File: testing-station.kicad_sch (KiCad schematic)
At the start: 12 parts, among them J1 pyranometer, J2 anemometer, J3 AM2315C, J4 FPC connector, U1 TBA_1-0519

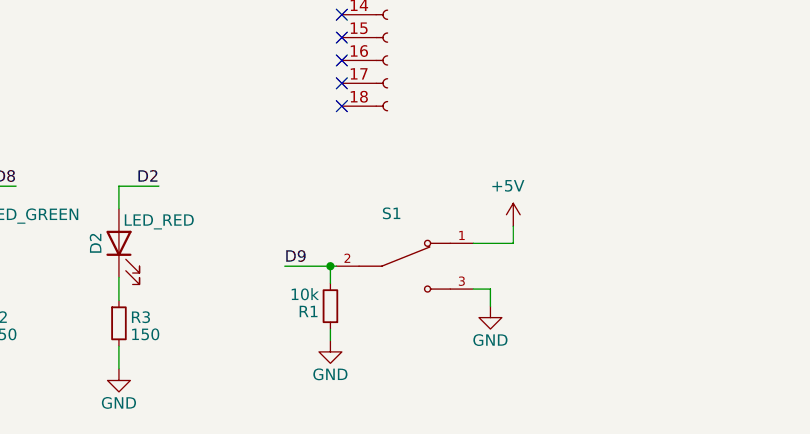
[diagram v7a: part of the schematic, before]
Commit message: added missing external files for PSU and switch + footprints update
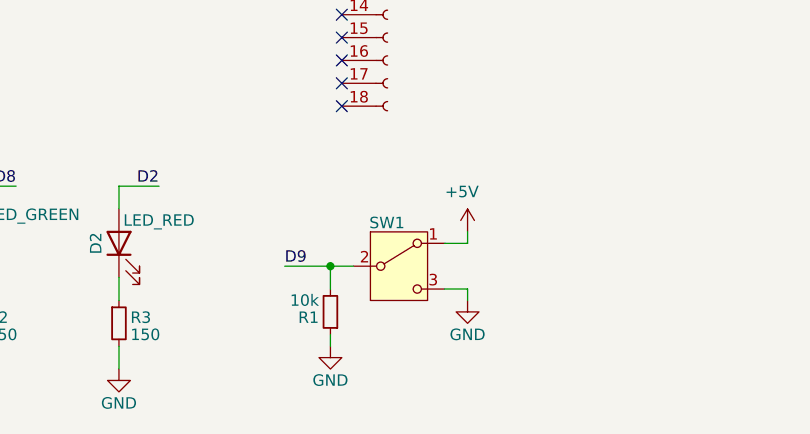
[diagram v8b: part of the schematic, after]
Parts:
- J1, J3: footprint custom_components:screw_terminal_4pin -> TerminalBlock:TerminalBlock_bornier-4_P5.08mm
- J2: footprint custom_components:screw_terminal_3pin -> TerminalBlock:TerminalBlock_bornier-3_P5.08mm
- SW1: renamed from S1; footprint 500SSP1S2M2QEA:SW_500SSP1S2M2QEA -> external_footprints:500SSP1S2M2QEA; symbol 500SSP1S2M2QEA:500SSP1S2M2QEA -> Switch:SW_SPDT
- U1: footprint TBA_1-0519:CONV_TBA_1-0519 -> external_footprints:TBA_1-0519
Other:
- moved on the sheet: R1, SW1
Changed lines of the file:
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@@
 	(wire
 		(pts
-			(xy 131.445 152.4) (xy 135.89 152.4)
-		)
-		(stroke
-			(width 0)
-			(type default)
-			(color 255 0 0 1)
-		)
-	)
-	(wire
-		(pts
 			(xy 110.49 109.22) (xy 116.84 109.22)
 		)
@@
 	(wire
 		(pts
-			(xy 115.57 154.94) (xy 116.205 154.94)
+			(xy 128.27 157.48) (xy 130.81 157.48)
 		)
 		(stroke
 			(width 0)
 			(type default)
-			(color 0 0 255 1)
+			(color 0 0 0 1)
 		)
 	)
@@
 	(wire
 		(pts
-			(xy 131.445 157.48) (xy 133.35 157.48)
-		)
-		(stroke
-			(width 0)
-			(type default)
-			(color 0 0 0 1)
-		)
-	)
-	(wire
-		(pts
 			(xy 110.49 50.8) (xy 116.84 50.8)
 		)
@@
 	(wire
 		(pts
+			(xy 115.57 154.94) (xy 115.57 157.48)
+		)
+		(stroke
+			(width 0)
+			(type default)
+			(color 0 0 255 1)
+		)
+	)
+	(wire
+		(pts
 			(xy 83.82 69.85) (xy 88.9 69.85)
 		)
@@
 	(wire
 		(pts
-			(xy 135.89 152.4) (xy 135.89 150.495)
+			(xy 130.81 152.4) (xy 130.81 151.13)
 		)
 		(stroke
@@
 	(wire
 		(pts
-			(xy 115.57 163.195) (xy 115.57 161.925)
+			(xy 115.57 163.83) (xy 115.57 162.56)
 		)
 		(stroke
@@
 	(wire
 		(pts
-			(xy 49.53 102.87) (xy 44.45 102.87)
+			(xy 115.57 154.94) (xy 118.11 154.94)
+		)
+		(stroke
+			(width 0)
+			(type default)
+			(color 0 0 255 1)
+		)
+	)
+	(wire
+		(pts
+			(xy 128.27 152.4) (xy 130.81 152.4)
 		)
 		(stroke
@@
 	(wire
 		(pts
-			(xy 114.3 93.98) (xy 116.84 93.98)
+			(xy 49.53 102.87) (xy 44.45 102.87)
 		)
 		(stroke
@@
 	(wire
 		(pts
-			(xy 115.57 154.94) (xy 115.57 156.845)
+			(xy 114.3 93.98) (xy 116.84 93.98)
 		)
 		(stroke
 			(width 0)
 			(type default)
-			(color 0 0 255 1)
+			(color 255 0 0 1)
 		)
 	)
@@
 	(wire
 		(pts
+			(xy 130.81 157.48) (xy 130.81 158.75)
+		)
+		(stroke
+			(width 0)
+			(type default)
+			(color 0 0 0 1)
+		)
+	)
+	(wire
+		(pts
 			(xy 38.1 154.94) (xy 35.56 154.94)
 		)
@@
 		)
 	)
-	(wire
-		(pts
-			(xy 133.35 157.48) (xy 133.35 159.385)
-		)
-		(stroke
-			(width 0)
-			(type default)
-			(color 0 0 0 1)
-		)
-	)
 	(label "SCK"
 		(at 110.49 101.6 0)
@@
 			)
 		)
-		(property "Footprint" "custom_components:screw_terminal_4pin"
+		(property "Footprint" "TerminalBlock:TerminalBlock_bornier-4_P5.08mm"
 			(at 96.52 102.87 0)
 			(effects
@@
 			)
 		)
-		(property "Footprint" "custom_components:screw_terminal_4pin"
+		(property "Footprint" "TerminalBlock:TerminalBlock_bornier-4_P5.08mm"
 			(at 54.61 102.87 0)
 			(effects
@@
 			)
 		)
-		(property "Footprint" "TBA_1-0519:CONV_TBA_1-0519"
+		(property "Footprint" "external_footprints:TBA_1-0519"
 			(at 40.64 158.75 0)
 			(effects
@@
 	(symbol
 		(lib_id "power:+5V")
-		(at 135.89 150.495 0)
+		(at 130.81 151.13 0)
 		(unit 1)
 		(exclude_from_sim no)
@@
 		(dnp no)
 		(property "Reference" "#PWR09"
-			(at 135.89 154.305 0)
+			(at 130.81 154.94 0)
 			(effects
 				(font
@@
 		)
 		(property "Value" "+5V"
-			(at 135.255 146.05 0)
+			(at 130.175 146.685 0)
 			(effects
 				(font
@@
 		)
 		(property "Footprint" ""
-			(at 135.89 150.495 0)
+			(at 130.81 151.13 0)
 			(effects
 				(font
@@
 		)
 		(property "Datasheet" ""
-			(at 135.89 150.495 0)
+			(at 130.81 151.13 0)
 			(effects
 				(font
@@
 		)
 		(property "Description" ""
-			(at 135.89 150.495 0)
+			(at 130.81 151.13 0)
 			(effects
 				(font
@@
 	)
 	(symbol
-		(lib_id "500SSP1S2M2QEA:500SSP1S2M2QEA")
-		(at 123.825 154.94 0)
+		(lib_id "Switch:SW_SPDT")
+		(at 123.19 154.94 0)
 		(unit 1)
-		(exclude_from_sim yes)
+		(exclude_from_sim no)
 		(in_bom yes)
 		(on_board yes)
 		(dnp no)
-		(property "Reference" "S1"
-			(at 121.285 149.86 0)
+		(property "Reference" "SW1"
+			(at 119.888 150.876 0)
 			(effects
 				(font
@@
 		)
 		(property "Value" "500SSP1S2M2QEA"
-			(at 113.665 146.05 0)
+			(at 113.03 146.05 0)
 			(effects
 				(font
@@
 			)
 		)
-		(property "Footprint" "500SSP1S2M2QEA:SW_500SSP1S2M2QEA"
-			(at 123.825 154.94 0)
+		(property "Footprint" "external_footprints:500SSP1S2M2QEA"
+			(at 123.19 154.94 0)
 			(effects
 				(font
 					(size 1.27 1.27)
 				)
-				(justify bottom)
 				(hide yes)
 			)
 		)
-		(property "Datasheet" ""
-			(at 123.825 154.94 0)
+		(property "Datasheet" "~"
+			(at 123.19 162.56 0)
 			(effects
 				(font
@@
 			)
 		)
-		(property "Description" "Slide Switch"
-			(at 123.825 154.94 0)
+		(property "Description" "Switch, single pole double throw"
+			(at 123.19 154.94 0)
 			(effects
 				(font
@@
 		)
 		(property "Manufacturer" "E-switch"
-			(at 123.825 154.94 0)
+			(at 123.19 154.94 0)
 			(effects
 				(font
@@
 		)
 		(property "MPN" "500SSP1S2M2QEA"
-			(at 123.825 154.94 0)
+			(at 123.19 154.94 0)
 			(effects
 				(font
@@
 		)
 		(property "Supplier" "DigiKey"
-			(at 123.825 154.94 0)
+			(at 123.19 154.94 0)
 			(effects
 				(font
@@
 		)
 		(property "SPN" "EG5137-ND"
-			(at 123.825 154.94 0)
+			(at 123.19 154.94 0)
 			(effects
 				(font
@@
 			(project "testing-station"
 				(path "/ed3950ec-e24f-4dd6-b9cc-eca012f1333b"
-					(reference "S1")
+					(reference "SW1")
 					(unit 1)
 				)
@@
 	(symbol
 		(lib_id "power:GND")
-		(at 133.35 159.385 0)
+		(at 130.81 158.75 0)
 		(unit 1)
 		(exclude_from_sim no)
@@
 		(dnp no)
 		(property "Reference" "#PWR012"
-			(at 133.35 165.735 0)
+			(at 130.81 165.1 0)
 			(effects
 				(font
@@
 		)
 		(property "Value" "GND"
-			(at 133.35 163.195 0)
+			(at 130.81 162.56 0)
 			(effects
 				(font
@@
 		)
 		(property "Footprint" ""
-			(at 133.35 159.385 0)
+			(at 130.81 158.75 0)
 			(effects
 				(font
@@
 		)
 		(property "Datasheet" ""
-			(at 133.35 159.385 0)
+			(at 130.81 158.75 0)
 			(effects
 				(font
@@
 		)
 		(property "Description" ""
-			(at 133.35 159.385 0)
+			(at 130.81 158.75 0)
 			(effects
 				(font
@@
 	(symbol
 		(lib_id "power:GND")
-		(at 115.57 163.195 0)
+		(at 115.57 163.83 0)
 		(unit 1)
 		(exclude_from_sim no)
@@
 		(dnp no)
 		(property "Reference" "#PWR015"
-			(at 115.57 169.545 0)
+			(at 115.57 170.18 0)
 			(effects
 				(font
@@
 		)
 		(property "Value" "GND"
-			(at 115.57 167.005 0)
+			(at 115.57 167.64 0)
 			(effects
 				(font
@@
 		)
 		(property "Footprint" ""
-			(at 115.57 163.195 0)
+			(at 115.57 163.83 0)
 			(effects
 				(font
@@
 		)
 		(property "Datasheet" ""
-			(at 115.57 163.195 0)
+			(at 115.57 163.83 0)
 			(effects
 				(font
@@
 		)
 		(property "Description" ""
-			(at 115.57 163.195 0)
+			(at 115.57 163.83 0)
 			(effects
 				(font
@@
 			)
 		)
-		(property "Footprint" "custom_components:screw_terminal_3pin"
+		(property "Footprint" "TerminalBlock:TerminalBlock_bornier-3_P5.08mm"
 			(at 76.2 102.87 0)
 			(effects
@@
 	(symbol
 		(lib_id "Device:R_Small")
-		(at 115.57 159.385 180)
+		(at 115.57 160.02 180)
 		(unit 1)
 		(exclude_from_sim no)
@@
 		(dnp no)
 		(property "Reference" "R1"
-			(at 114.3 160.02 0)
+			(at 114.3 160.655 0)
 			(effects
 				(font
@@
 		)
 		(property "Value" "10k"
-			(at 114.3 158.115 0)
+			(at 114.3 158.75 0)
 			(effects
 				(font
@@
 		)
 		(property "Footprint" "Resistor_SMD:R_1206_3216Metric_Pad1.30x1.75mm_HandSolder"
-			(at 115.57 159.385 0)
+			(at 115.57 160.02 0)
 			(effects
 				(font
@@
 		)
 		(property "Datasheet" ""
-			(at 115.57 159.385 0)
+			(at 115.57 160.02 0)
 			(effects
 				(font
@@
 		)
 		(property "Description" "SMD Chip Resistor, 10 kohm, ± 1%, 250 mW, 1206 [3216 Metric], Thick Film, General Purpose"
-			(at 115.57 159.385 0)
+			(at 115.57 160.02 0)
 			(effects
 				(font
@@
 		)
 		(property "Manufacturer" "/"
-			(at 115.57 159.385 0)
+			(at 115.57 160.02 0)
 			(effects
 				(font
@@
 		)
 		(property "MPN" "/"
-			(at 115.57 159.385 0)
+			(at 115.57 160.02 0)
 			(effects
 				(font
@@
 		)
 		(property "Supplier" "Eurocircuits"
-			(at 115.57 159.385 0)
+			(at 115.57 160.02 0)
 			(effects
 				(font
@@
 		)
 		(property "SPN" "GPR120610K"
-			(at 115.57 159.385 0)
+			(at 115.57 160.02 0)
 			(effects
 				(font
@@
 		)
 		(property "Component package type" "R_1206"
-			(at 115.57 159.385 0)
+			(at 115.57 160.02 0)
 			(effects
 				(font
